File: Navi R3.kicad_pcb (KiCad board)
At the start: 4 copper layers, 40 x 60 mm, 68 parts, among them J1 USB_C_Receptacle_USB2.0_16P, J2 Conn_01x02_Pin, J3 Conn_01x02_Pin, J5 Conn_02x03_Counter_Clockwise, SW2 D2FC-F-7N20M, SW3 D2FC-F-7N20M, SW4 D2FC-F-7N20M, SW6 SW_Push, U1 MCP73833-xxx-UN, U2 nRF52820-QDxx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

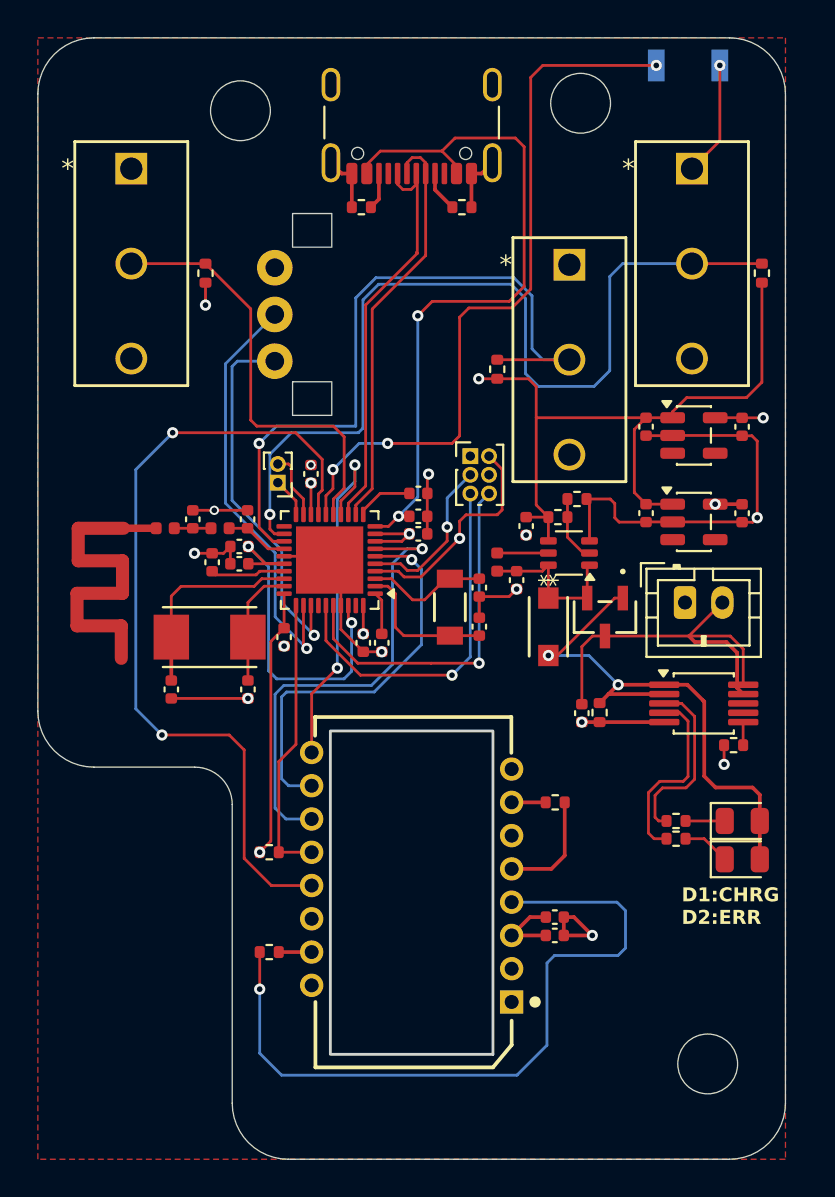
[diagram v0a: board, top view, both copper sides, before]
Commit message: Update SWD headers
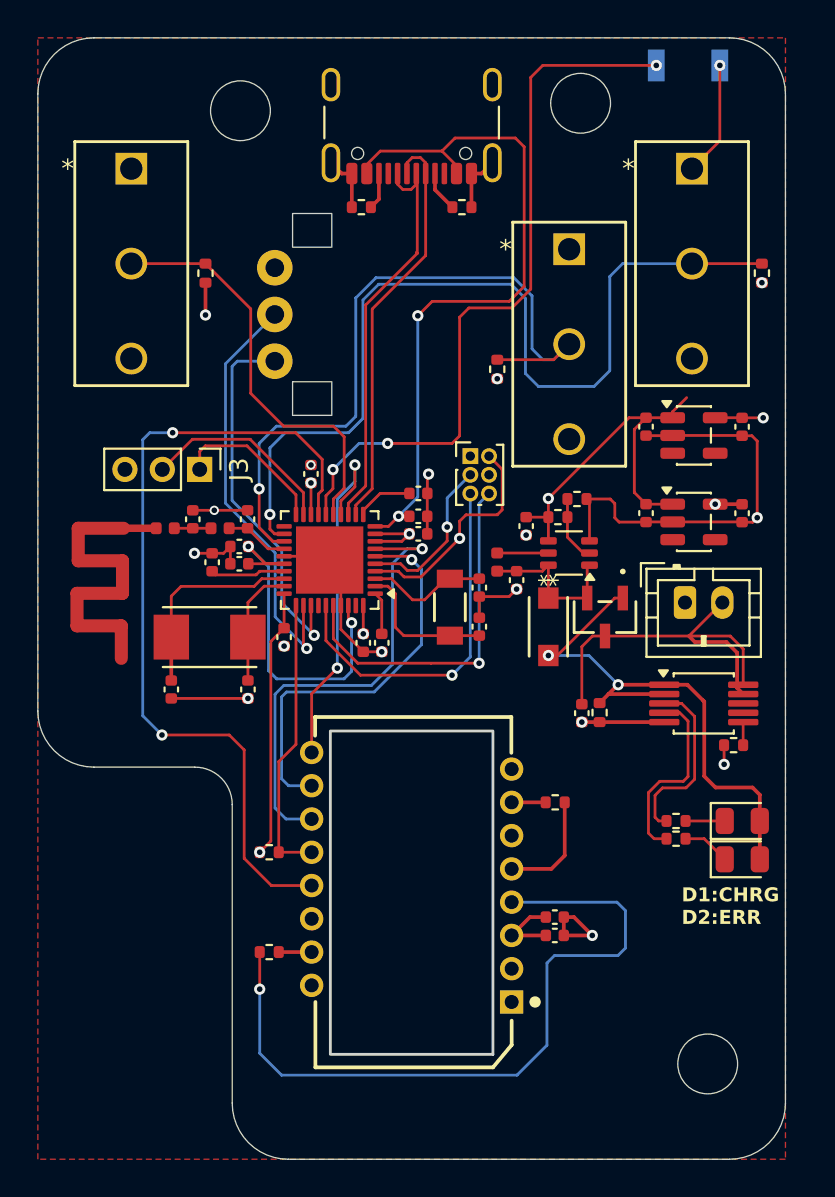
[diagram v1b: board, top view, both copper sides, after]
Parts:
- J3: value Conn_01x02_Pin -> Conn_01x03_Pin; footprint Connector_PinHeader_1.00mm:PinHeader_1x02_P1.00mm_Vertical -> Connector_PinHeader_2.00mm:PinHeader_1x03_P2.00mm_Vertical
- R15, R7, R8: value 10k -> 4.7k
- moved J3 4.24 mm to (166.0, 79.2), turned to -90 degrees
- moved SW4 0.83 mm to (185.8, 67.4)
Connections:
- R15 pad 1: +5V -> VDD
- R7 pad 1: +5V -> VDD
- R8 pad 1: +5V -> VDD
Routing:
- net VDD: track 29.9 -> 76.8 mm, vias 5 -> 8
- net +5V: track 64.0 -> 27.2 mm, vias 2 -> 1
- net /SWDIO: track 3.61 -> 10.6 mm
- net /SWDCLK: track 2.10 -> 8.37 mm
- net /P0.15: track 23.1 -> 22.3 mm

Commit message: Update rules for DRC
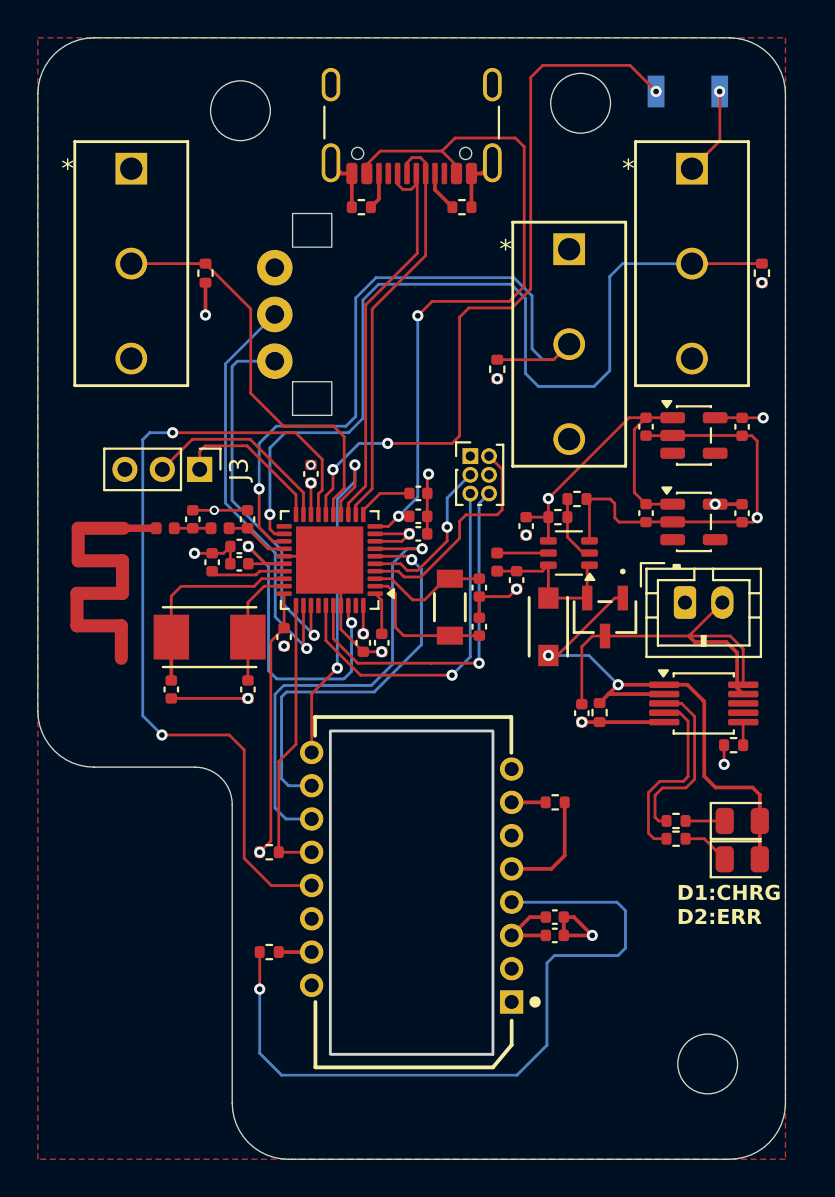
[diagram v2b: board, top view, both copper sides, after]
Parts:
- moved SW6 1.40 mm to (192.1, 59.0)
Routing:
- net B-: track 75.8 -> 74.4 mm
- net +5V: track 27.2 -> 25.8 mm
- net /P0.18/~{RESET}: track 39.2 -> 39.7 mm
- net /AIN2/P0.04: vias 1 -> 0
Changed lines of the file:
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@@
 		)
 		(fp_text user "*"
-			(at -2.4892 0 270)
-			(unlocked yes)
-			(layer "F.SilkS")
-			(effects
-				(font
-					(size 1 1)
-					(thickness 0.15)
-				)
-			)
-		)
-		(fp_text user "*"
-			(at -2.4892 0 90)
-			(layer "F.SilkS")
-			(effects
-				(font
-					(size 1 1)
-					(thickness 0.15)
-				)
-			)
-		)
-		(fp_text user "*"
 			(at -1.1938 0 270)
 			(unlocked yes)
@@
 	(footprint "Button_Switch_SMD:SW_SPST_B3U-3000P"
 		(layer "B.Cu")
-		(at 192.15 57.575 180)
+		(at 192.14 58.97 180)
 		(descr "Ultra-small-sized Tactile Switch with High Contact Reliability, Side-actuated Model, without Ground Terminal, without Boss")
 		(tags "Tactile Switch")
@@
 	)
 	(gr_text "D1:CHRG\nD2:ERR"
-		(at 191.8 103.6 0)
+		(at 191.55 103.61 0)
 		(layer "F.SilkS")
 		(effects
 			(font
-				(size 0.75 0.75)
-				(thickness 0.15)
+				(size 0.8 0.8)
+				(thickness 0.175)
 				(bold yes)
 			)
@@
 	)
 	(segment
-		(start 166.8 81.379)
-		(end 168.58 81.379)
-		(width 0.15)
-		(layer "F.Cu")
-		(net 1)
-	)
-	(segment
 		(start 191.325 82)
 		(end 189.91 82)
@@
 	)
 	(segment
-		(start 193.85 61.61)
-		(end 192.36 63.1)
-		(width 0.15)
-		(layer "F.Cu")
-		(net 1)
-	)
-	(segment
 		(start 178.26 82.704)
 		(end 178.195 82.639)
@@
 	)
 	(segment
-		(start 168.0005 81.379)
-		(end 168 81.3785)
-		(width 0.15)
-		(layer "F.Cu")
-		(net 1)
-	)
-	(segment
 		(start 195.04 77.39)
 		(end 195.565 77.39)
@@
 	)
 	(segment
+		(start 193.84 58.97)
+		(end 193.85 58.98)
+		(width 0.15)
+		(layer "F.Cu")
+		(net 1)
+	)
+	(segment
 		(start 189.91 82)
 		(end 189.9 82.01)
@@
 	)
 	(segment
+		(start 193.85 61.61)
+		(end 192.36 63.1)
+		(width 0.15)
+		(layer "F.Cu")
+		(net 1)
+	)
+	(segment
 		(start 178.2 79.505)
 		(end 178.265 79.44)
@@
 	)
 	(segment
+		(start 193.85 58.98)
+		(end 193.85 61.61)
+		(width 0.15)
+		(layer "F.Cu")
+		(net 1)
+	)
+	(segment
 		(start 186.8758 83.014)
 		(end 186.8758 80.934)
@@
 	)
 	(segment
-		(start 188.23 81.78)
-		(end 188.46 82.01)
+		(start 166.8 81.379)
+		(end 168.58 81.379)
 		(width 0.15)
 		(layer "F.Cu")
@@
 	)
 	(segment
-		(start 193.85 57.575)
-		(end 193.85 61.61)
+		(start 188.23 81.78)
+		(end 188.46 82.01)
 		(width 0.15)
 		(layer "F.Cu")
@@
 	)
 	(via
-		(at 193.85 57.575)
+		(at 193.84 58.97)
 		(size 0.6)
 		(drill 0.3)
@@
 	)
 	(segment
+		(start 192.1115 90.7115)
+		(end 192.955 91.555)
+		(width 0.2)
+		(layer "F.Cu")
+		(net 3)
+	)
+	(segment
 		(start 187.4158 91.6915)
 		(end 187.8958 91.2115)
@@
 	)
 	(segment
-		(start 192.1115 90.7115)
-		(end 193.015 91.615)
-		(width 0.2)
-		(layer "F.Cu")
-		(net 3)
-	)
-	(segment
 		(start 177.69 70.97)
 		(end 178.46 70.2)
@@
 	)
 	(segment
-		(start 190.8758 90.7115)
-		(end 192.1115 90.7115)
-		(width 0.2)
-		(layer "F.Cu")
-		(net 3)
-	)
-	(segment
 		(start 185.1547 89.1474)
 		(end 184.6758 89.1474)
@@
 		(net 3)
 	)
+	(segment
+		(start 190.8758 90.7115)
+		(end 192.1115 90.7115)
+		(width 0.2)
+		(layer "F.Cu")
+		(net 3)
+	)
 	(via
 		(at 184.6758 89.1474)
@@
 	)
 	(segment
-		(start 192.075 75.35)
-		(end 191.325 76.1)
-		(width 0.15)
-		(layer "F.Cu")
-		(net 18)
-	)
-	(segment
 		(start 184.6758 81.744)
 		(end 183.316 81.744)
@@
 		(net 18)
 	)
-	(segment
-		(start 191.325 76.1)
-		(end 191.325 76.425)
-		(width 0.15)
-		(layer "F.Cu")
-		(net 18)
-	)
 	(via
 		(at 184.6758 80.7442)
@@
 	)
 	(segment
-		(start 177.61 67.582156)
-		(end 177.66 67.632156)
-		(width 0.15)
-		(layer "F.Cu")
-		(net 25)
-	)
-	(segment
 		(start 176.61 63.36)
 		(end 176.61 63.934999)
@@
 	)
 	(segment
-		(start 182.725388 70.551)
-		(end 183.731 69.545388)
+		(start 179.925 77.395)
+		(end 179.925 71.05)
 		(width 0.15)
 		(layer "F.Cu")
@@
 	)
 	(segment
-		(start 179.925 77.395)
-		(end 179.925 71.05)
+		(start 172.7725 80.6025)
+		(end 173.15 80.225)
 		(width 0.15)
 		(layer "F.Cu")
@@
 	)
 	(segment
-		(start 183.731 69.545388)
-		(end 183.731 58.219)
+		(start 172.7725 81.6015)
+		(end 172.7725 80.6025)
 		(width 0.15)
 		(layer "F.Cu")
@@
 	)
 	(segment
-		(start 179.925 71.05)
-		(end 180.424 70.551)
+		(start 183.731 58.219)
+		(end 184.375 57.575)
 		(width 0.15)
 		(layer "F.Cu")
@@
 	)
 	(segment
-		(start 184.375 57.575)
-		(end 190.45 57.575)
+		(start 179.925 71.05)
+		(end 180.424 70.551)
 		(width 0.15)
 		(layer "F.Cu")
@@
 	)
 	(segment
-		(start 183.731 58.219)
-		(end 184.375 57.575)
+		(start 179.52 77.8)
+		(end 179.925 77.395)
 		(width 0.15)
 		(layer "F.Cu")
@@
 	)
 	(segment
-		(start 172.7725 80.6025)
-		(end 173.15 80.225)
+		(start 183.731 69.545388)
+		(end 183.731 58.219)
 		(width 0.15)
 		(layer "F.Cu")
@@
 	)
 	(segment
-		(start 179.52 77.8)
-		(end 179.925 77.395)
+		(start 189.045 57.575)
+		(end 190.44 58.97)
 		(width 0.15)
 		(layer "F.Cu")
@@
 	)
 	(segment
-		(start 172.7725 81.6015)
-		(end 172.7725 80.6025)
+		(start 173.15 80.225)
+		(end 173.15 79.2)
 		(width 0.15)
 		(layer "F.Cu")
@@
 	)
 	(segment
-		(start 180.424 70.551)
-		(end 182.725388 70.551)
+		(start 184.375 57.575)
+		(end 189.045 57.575)
 		(width 0.15)
 		(layer "F.Cu")
@@
 	)
 	(segment
-		(start 173.15 80.225)
-		(end 173.15 79.2)
+		(start 182.725388 70.551)
+		(end 183.731 69.545388)
+		(width 0.15)
+		(layer "F.Cu")
+		(net 30)
+	)
+	(segment
+		(start 180.424 70.551)
+		(end 182.725388 70.551)
 		(width 0.15)
 		(layer "F.Cu")
@@
 	)
 	(via
-		(at 190.45 57.575)
+		(at 190.44 58.97)
 		(size 0.6)
 		(drill 0.3)
@@
 		(net 46)
 	)
-	(via
-		(at 179.925 82.88)
-		(size 0.6)
-		(drill 0.3)
-		(layers "F.Cu" "B.Cu")
-		(net 46)
-	)
